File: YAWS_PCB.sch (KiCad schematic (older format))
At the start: 35 parts, among them J1 Conn_01x02_Male, J3 Conn_02x03_Odd_Even, J4 Conn_01x03, J5 Conn_01x02_Male, J6 Conn_01x02_Male, J7 Conn_01x04, Q1 BSS138, Q2 BSS138, U1 TP4056, U2 LT1763-3.3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

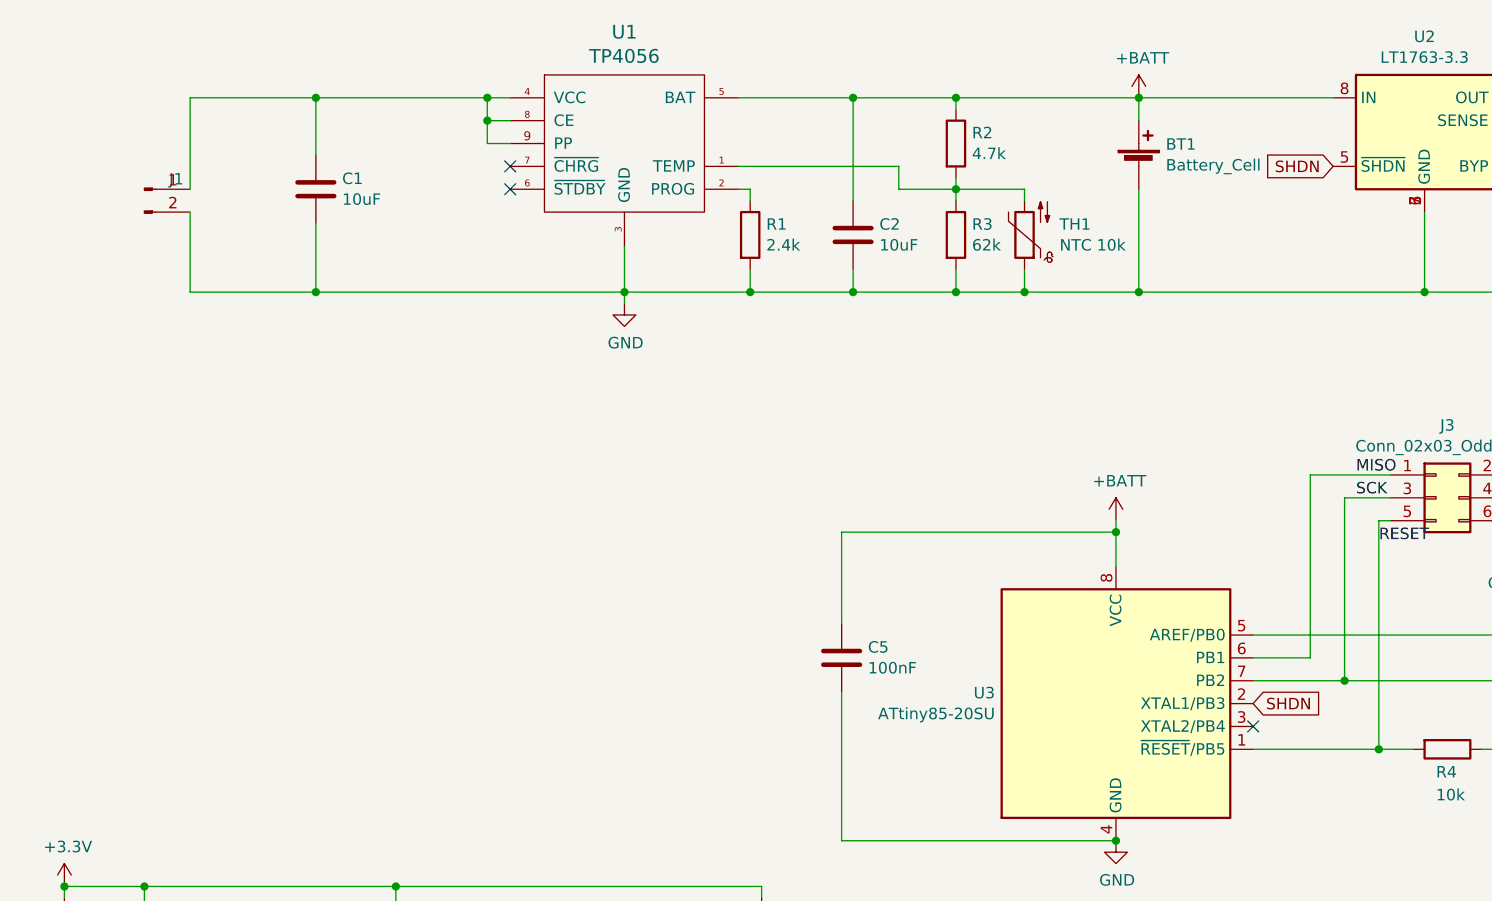
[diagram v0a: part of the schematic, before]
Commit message: added MOSFET to disconnect TP4056 from battery
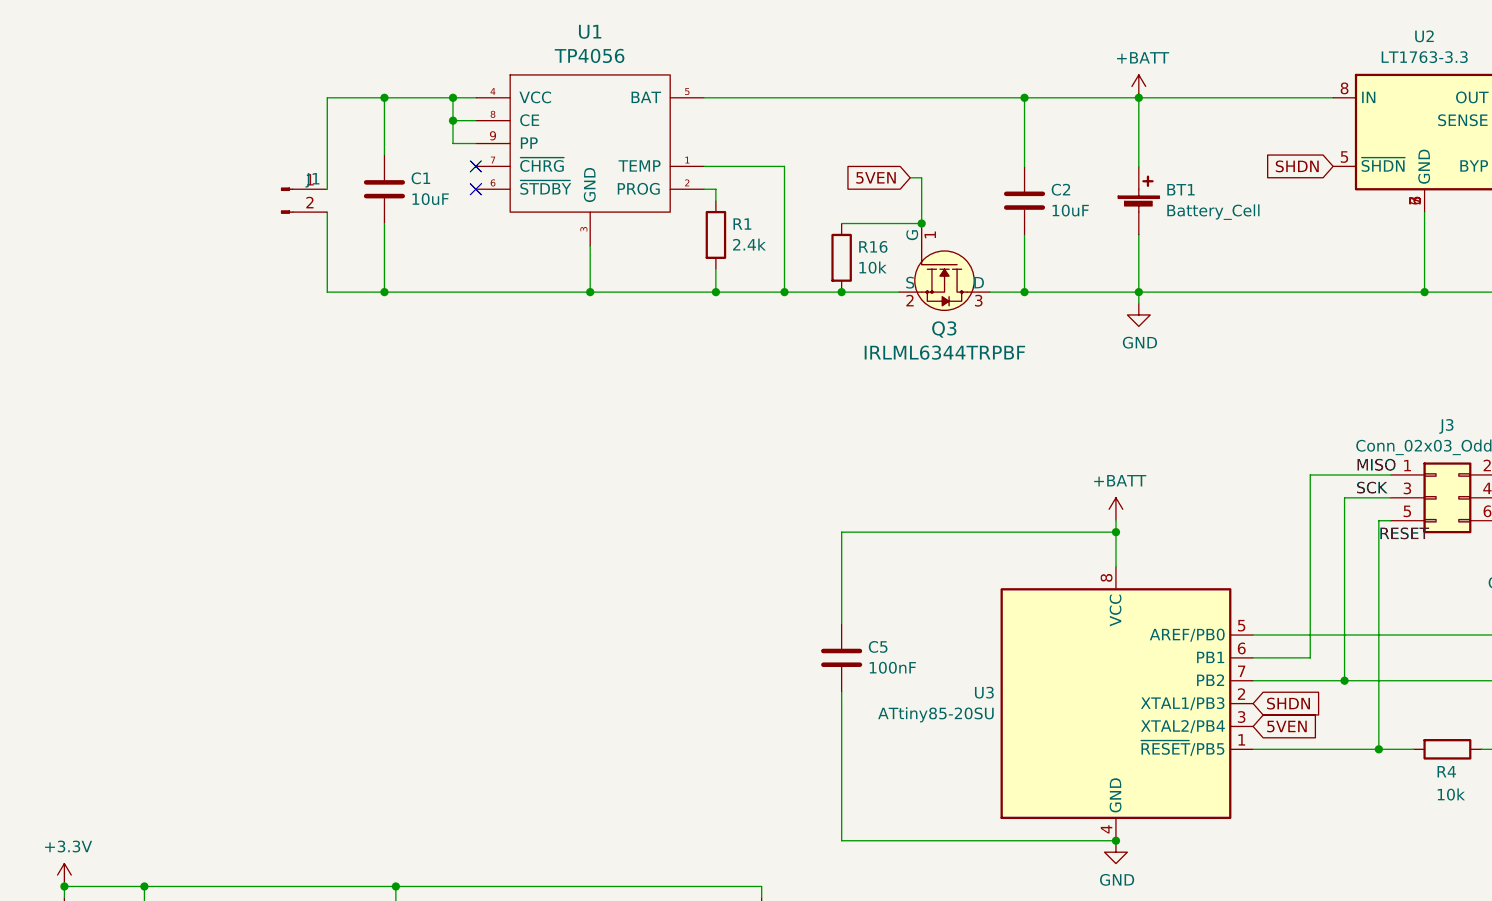
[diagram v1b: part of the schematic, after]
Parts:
- removed R2: 4.7k, Resistor_SMD:R_0805_2012Metric, symbol Device:R
- removed R3: 62k, Resistor_SMD:R_0805_2012Metric, symbol Device:R
- removed TH1: NTC 10k, Resistor_SMD:R_0805_2012Metric, symbol Device:Thermistor_NTC
- added Q3: IRLML6344TRPBF, digikey-footprints:SOT-23-3, symbol dk_Transistors-FETs-MOSFETs-Single:IRLML6344TRPBF
- added R16: 10k, Resistor_SMD:R_0805_2012Metric, symbol Device:R
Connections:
- net GND: now also Q3.3 (D); no longer C1.2, J1.2 (Pin_2), R1.2, U1.3 (GND)
- net at U1.1 (TEMP): now also C1.2, J1.2 (Pin_2), R1.2, U1.3 (GND), Q3.2 (S), R16.2
- net 5VEN: now reaches U3.3 (XTAL2/PB4)
- net 5VEN: now also Q3.1 (G), R16.1
- no-connect marks 16 -> 15
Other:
- moved on the sheet: BT1, C1, C2, J1, R1, U1

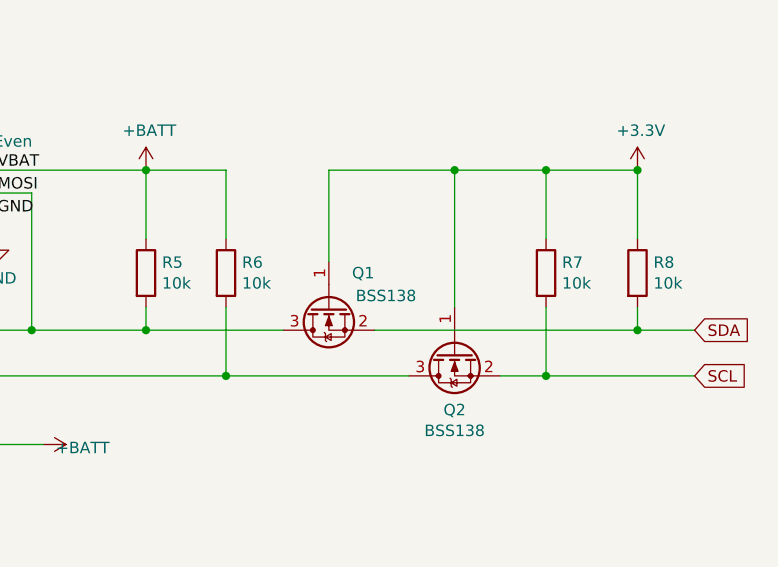
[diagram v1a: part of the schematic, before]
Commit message: reduced I2C pullups
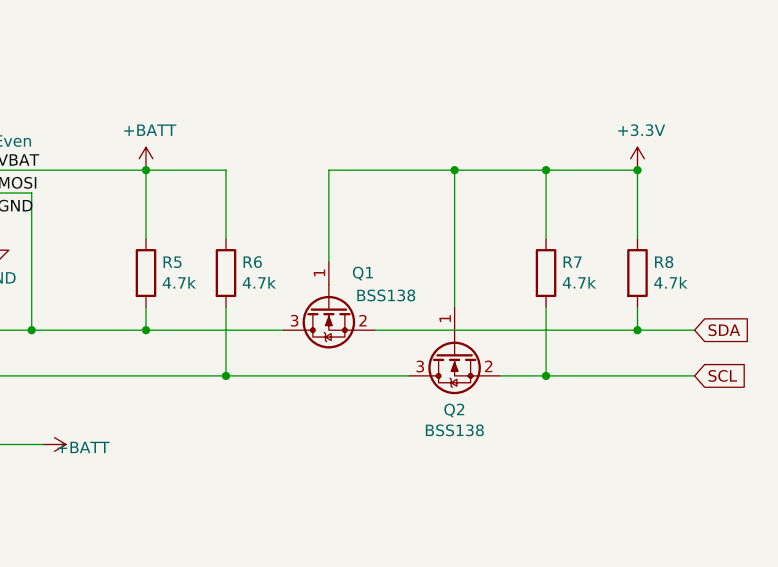
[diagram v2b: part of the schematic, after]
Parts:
- R5, R6, R7, R8: value 10k -> 4.7k
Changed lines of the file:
@@
 P 8150 3400
 F 0 "R5" H 8220 3446 50  0000 L CNN
-F 1 "10k" H 8220 3355 50  0000 L CNN
+F 1 "4.7k" H 8220 3355 50  0000 L CNN
 F 2 "Resistor_SMD:R_0805_2012Metric" V 8080 3400 50  0001 C CNN
 F 3 "~" H 8150 3400 50  0001 C CNN
@@
 P 8500 3400
 F 0 "R6" H 8570 3446 50  0000 L CNN
-F 1 "10k" H 8570 3355 50  0000 L CNN
+F 1 "4.7k" H 8570 3355 50  0000 L CNN
 F 2 "Resistor_SMD:R_0805_2012Metric" V 8430 3400 50  0001 C CNN
 F 3 "~" H 8500 3400 50  0001 C CNN
@@
 P 9900 3400
 F 0 "R7" H 9970 3446 50  0000 L CNN
-F 1 "10k" H 9970 3355 50  0000 L CNN
+F 1 "4.7k" H 9970 3355 50  0000 L CNN
 F 2 "Resistor_SMD:R_0805_2012Metric" V 9830 3400 50  0001 C CNN
 F 3 "~" H 9900 3400 50  0001 C CNN
@@
 P 10300 3400
 F 0 "R8" H 10370 3446 50  0000 L CNN
-F 1 "10k" H 10370 3355 50  0000 L CNN
+F 1 "4.7k" H 10370 3355 50  0000 L CNN
 F 2 "Resistor_SMD:R_0805_2012Metric" V 10230 3400 50  0001 C CNN
 F 3 "~" H 10300 3400 50  0001 C CNN
